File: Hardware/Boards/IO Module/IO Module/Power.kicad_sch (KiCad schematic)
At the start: 78 parts, among them J1 USB_C_Receptacle, Q1 IRLML6244, Q2 IRLML6244, Q3 IRLML6244, U1 TPS25730D, U17 TPD4E02B04DQA, U2 INA700AYWFR, U26 TPD4E02B04DQA, U3 TPSM33625RDNR, U4 TPD2EUSB30A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

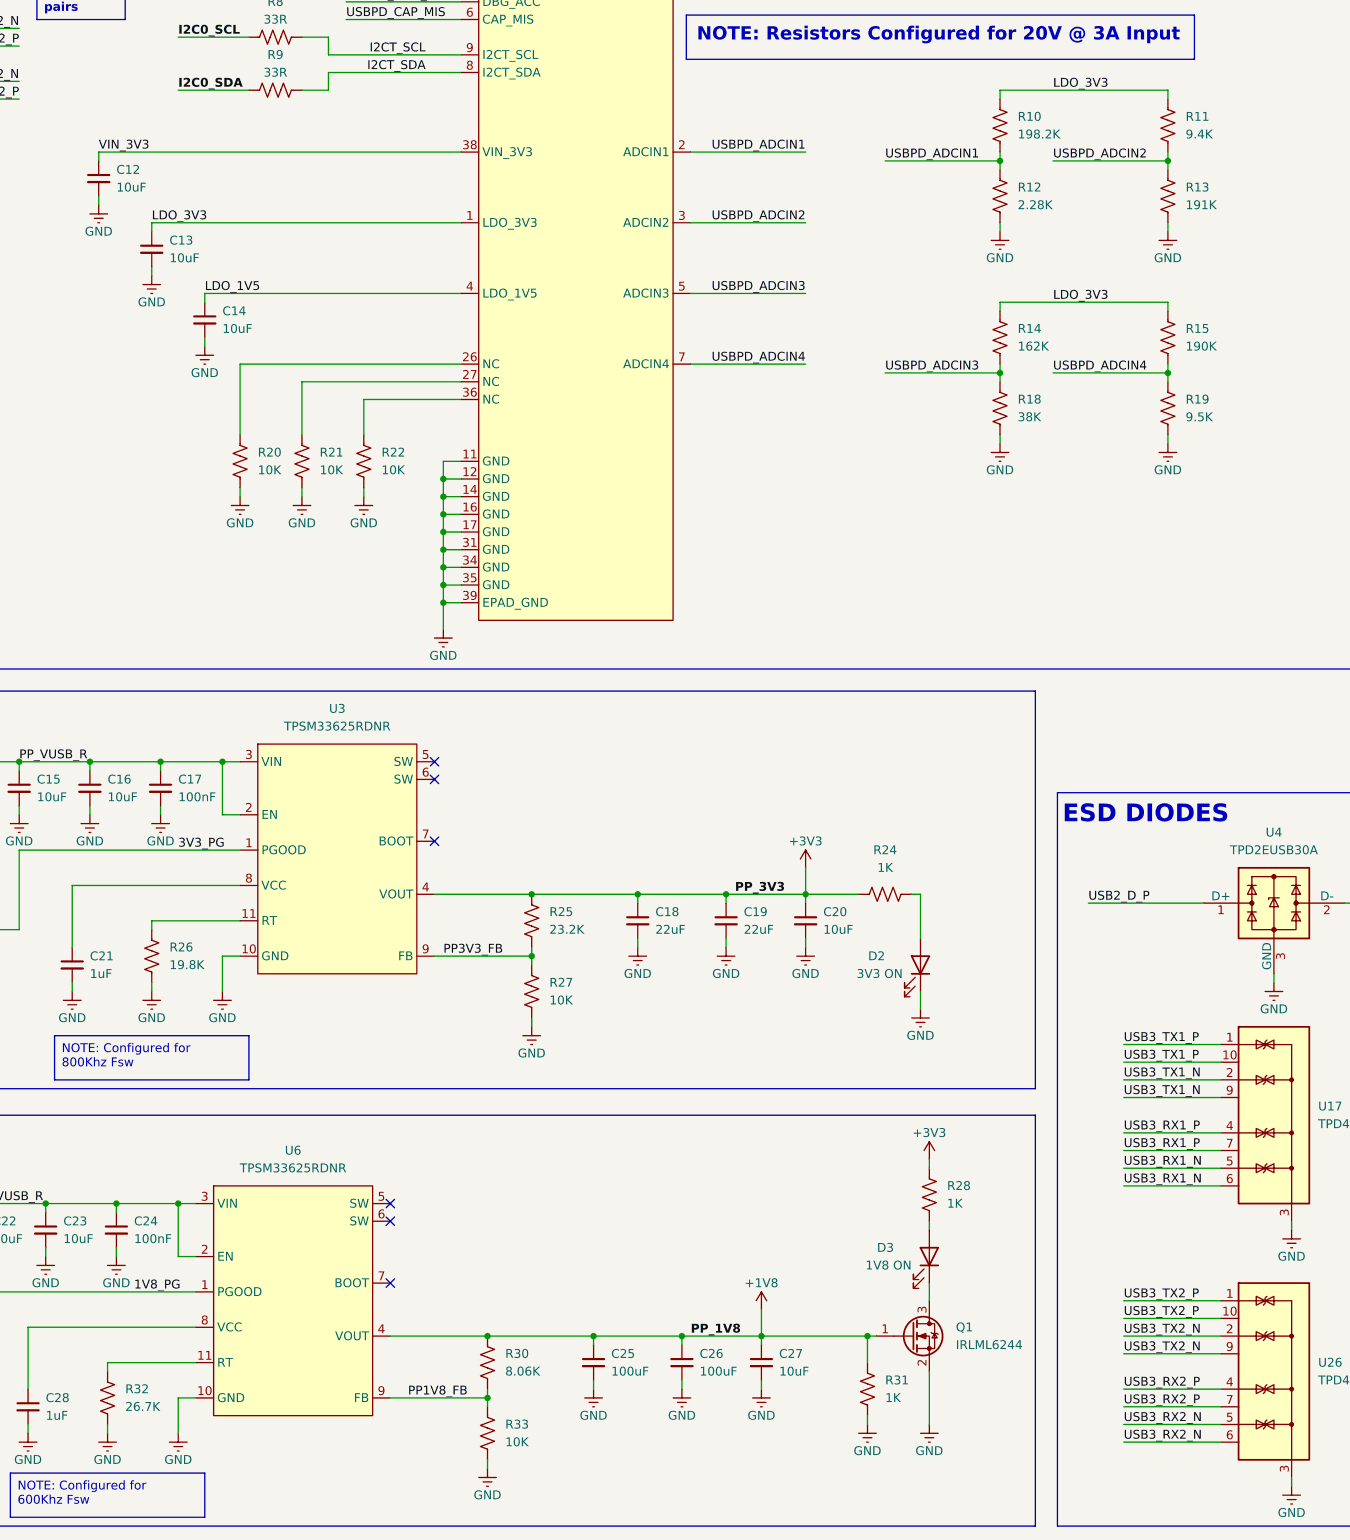
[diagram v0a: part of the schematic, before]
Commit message: Updated SCH and Layout
Added temp sensors for DCDC's, Added MCU control for FPGA mode, removed mode DIP switch
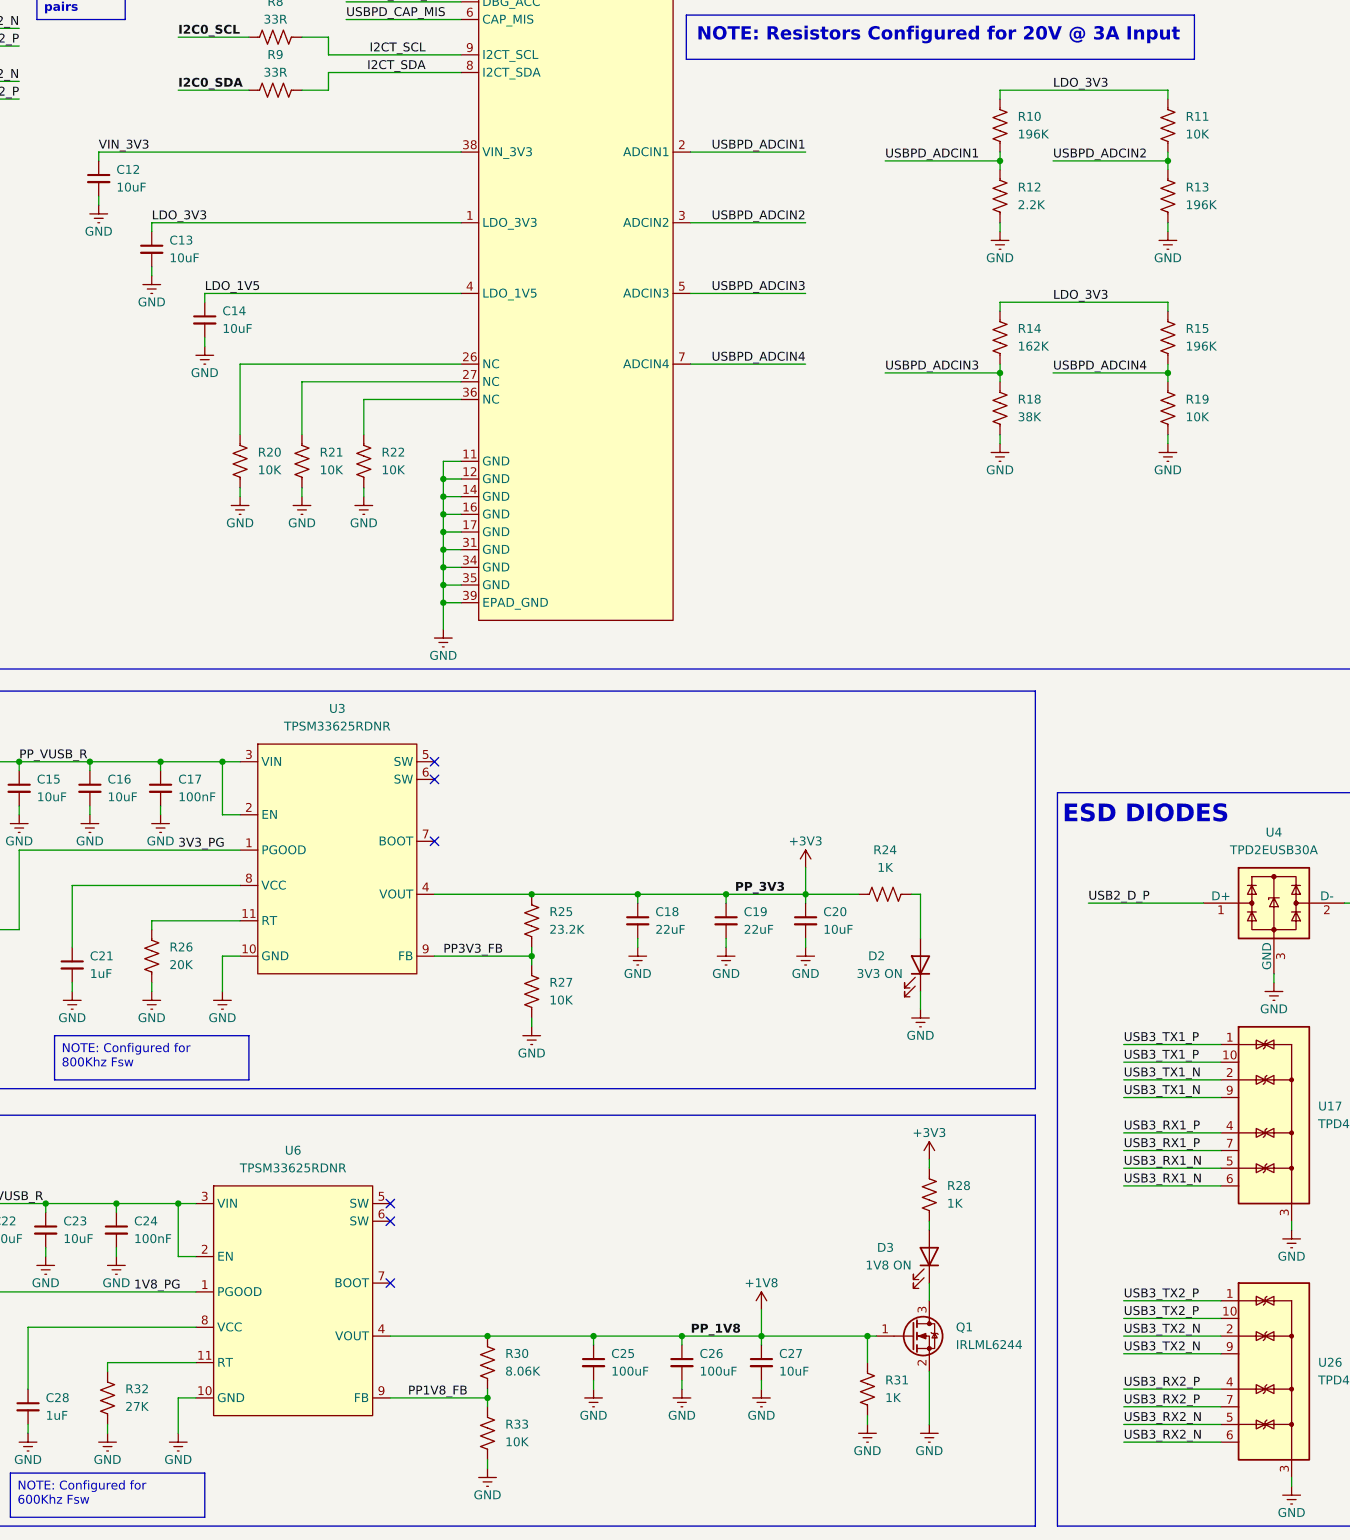
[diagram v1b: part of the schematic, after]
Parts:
- R10: value 198.2K -> 196K
- R11: value 9.4K -> 10K
- R12: value 2.28K -> 2.2K
- R13: value 191K -> 196K
- R15: value 190K -> 196K
- R19: value 9.5K -> 10K
- R26: value 19.8K -> 20K
- R32: value 26.7K -> 27K
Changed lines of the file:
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@@
 			)
 		)
-		(property "Value" "191K"
+		(property "Value" "196K"
 			(at 226.06 90.1699 0)
 			(effects
@@
 			)
 		)
-		(property "Value" "9.5K"
+		(property "Value" "10K"
 			(at 226.06 120.6499 0)
 			(effects
@@
 			)
 		)
-		(property "Value" "2.28K"
+		(property "Value" "2.2K"
 			(at 201.93 90.1699 0)
 			(effects
@@
 			)
 		)
-		(property "Value" "19.8K"
+		(property "Value" "20K"
 			(at 80.01 199.3899 0)
 			(effects
@@
 			)
 		)
-		(property "Value" "190K"
+		(property "Value" "196K"
 			(at 226.06 110.4899 0)
 			(effects
@@
 			)
 		)
-		(property "Value" "9.4K"
+		(property "Value" "10K"
 			(at 226.06 80.0099 0)
 			(effects
@@
 			)
 		)
-		(property "Value" "198.2K"
+		(property "Value" "196K"
 			(at 201.93 80.0099 0)
 			(effects
@@
 			)
 		)
-		(property "Value" "26.7K"
+		(property "Value" "27K"
 			(at 73.66 262.8899 0)
 			(effects

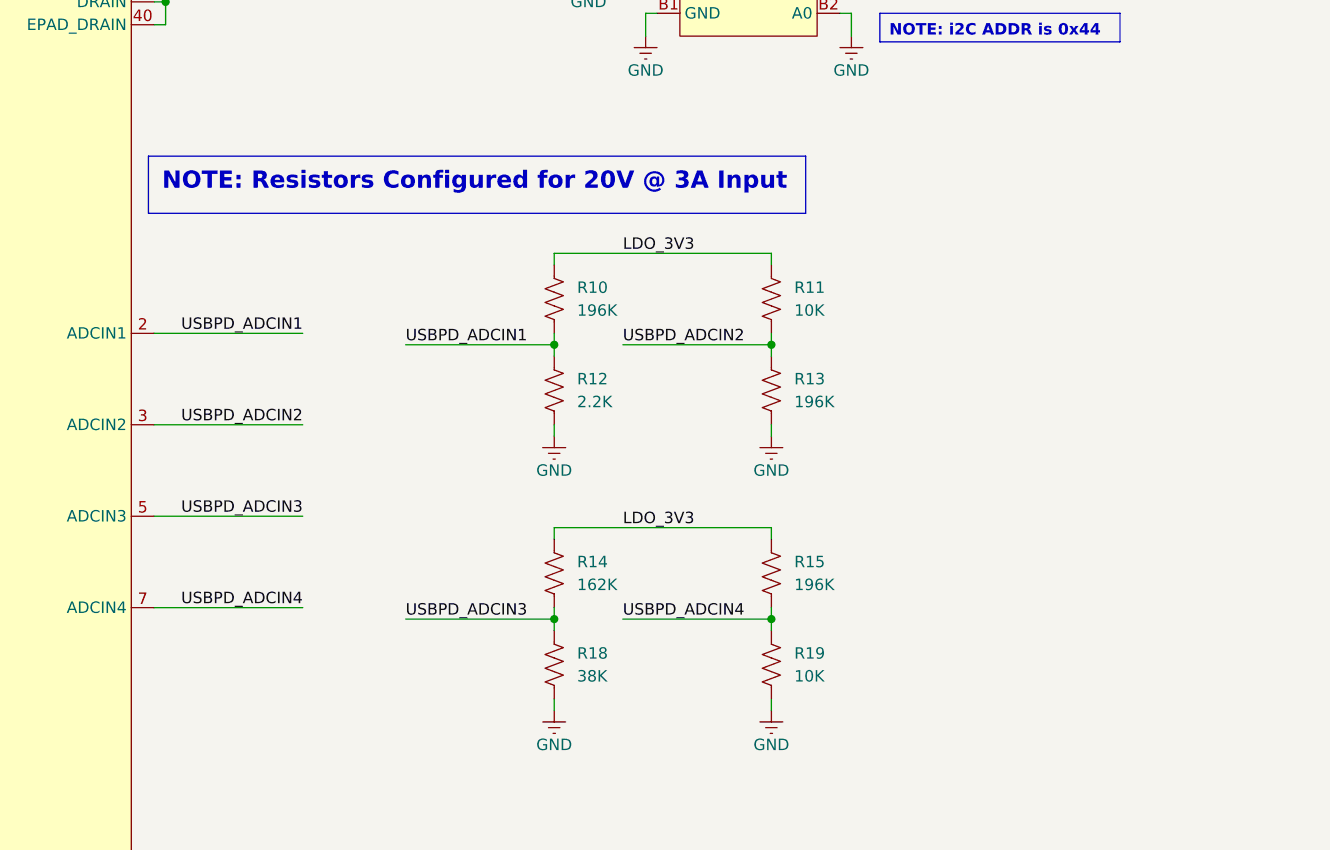
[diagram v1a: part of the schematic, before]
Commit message: FPGA Module Routing Updates
Modified DDR4 routing and FPGA IO Bus routing
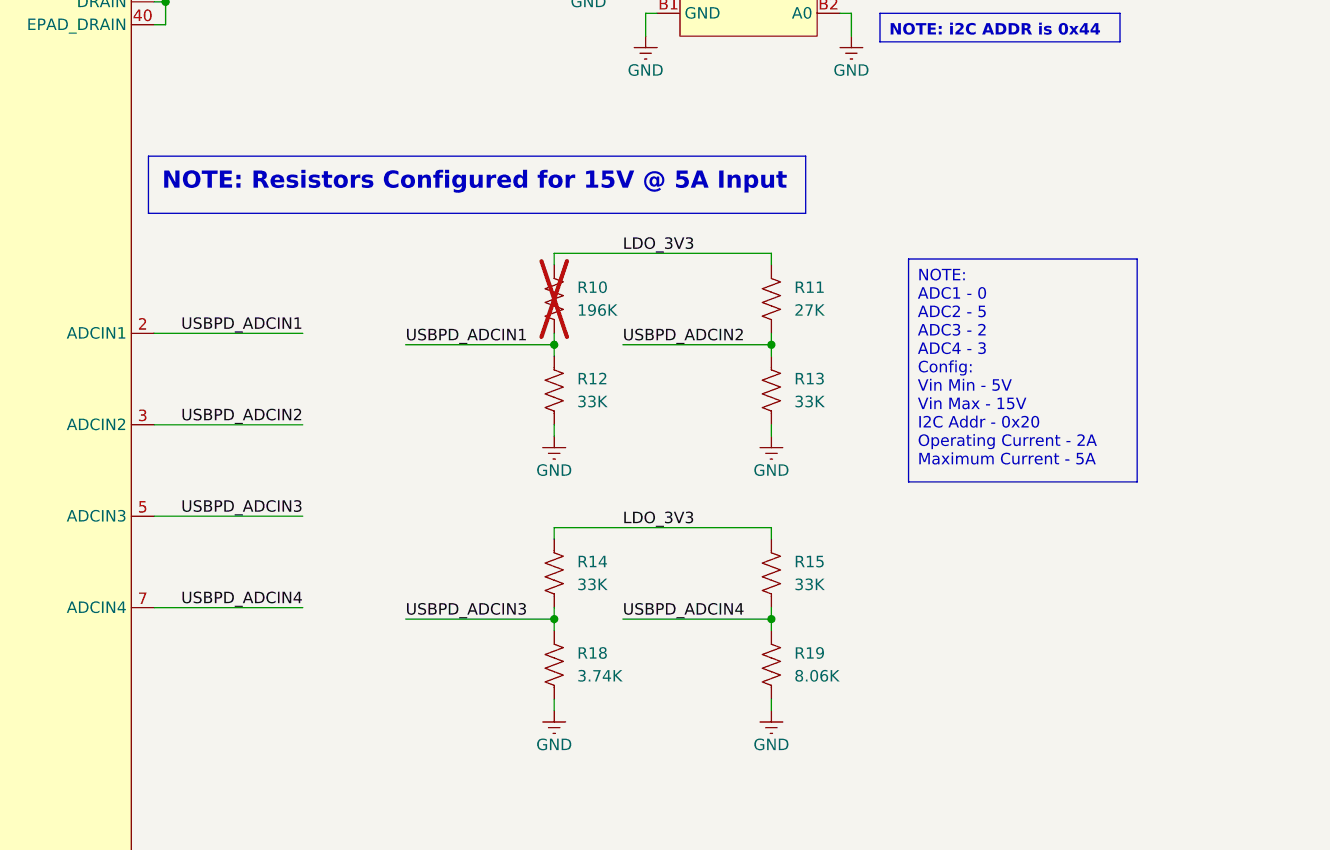
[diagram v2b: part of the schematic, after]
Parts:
- R10: now not fitted
- R11: value 10K -> 27K
- R12: value 2.2K -> 33K
- R13, R15: value 196K -> 33K
- R14: value 162K -> 33K
- R18: value 38K -> 3.74K
- R19: value 10K -> 8.06K
